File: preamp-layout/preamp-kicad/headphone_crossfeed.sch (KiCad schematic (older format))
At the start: 20 parts

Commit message: BOM Update
parts added to BOM, connector cleanup. Stopping point before renumbering refdes in a more intelligent way.
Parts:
- removed J? (x2): Conn_01x03_Female, Connector_PinHeader_2.54mm:PinHeader_1x03_P2.54mm_Vertical, symbol Connector:Conn_01x03_Female
- added J80, J81: Conn_01x04_Female, symbol Connector:Conn_01x04_Female
- C45, C48: renamed from C?; value 22nF -> 0.022uF
- C46, C47: renamed from C?; value 120nF -> 0.12uF
- gave numbers to parts that had none: 12
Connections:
- net GND: now also J81.2 (Pin_2)
- net L_IN: now also J80.1 (Pin_1)
- net L_OUT: now also J81.1 (Pin_1)
- net R_IN: now also J80.2 (Pin_2)
- net R_OUT: now also J81.3 (Pin_3)
- no-connect marks 0 -> 3

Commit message: Schematic Updates
Updated pin connections for DAC, footprint updates, MCU connections.
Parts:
- C45, C46, C47, C48: footprint (none) -> Capacitor_SMD:C_0805_2012Metric_Pad1.15x1.40mm_HandSolder
- J80, J81: footprint (none) -> Connector_PinHeader_2.54mm:PinHeader_1x04_P2.54mm_Vertical
- R80, R81, R82, R83, R84, R85, R86, R87, R88, R89: footprint (none) -> Resistor_SMD:R_1206_3216Metric_Pad1.42x1.75mm_HandSolder
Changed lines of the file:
@@
 F 0 "R81" H 3920 4196 50  0000 L CNN
 F 1 "1k" H 3920 4105 50  0000 L CNN
-F 2 "" V 3780 4150 50  0001 C CNN
+F 2 "Resistor_SMD:R_1206_3216Metric_Pad1.42x1.75mm_HandSolder" V 3780 4150 50  0001 C CNN
 F 3 "~" H 3850 4150 50  0001 C CNN
 	1    3850 4150
@@
 F 0 "R82" H 4420 3696 50  0000 L CNN
 F 1 "9.1k" H 4420 3605 50  0000 L CNN
-F 2 "" V 4280 3650 50  0001 C CNN
+F 2 "Resistor_SMD:R_1206_3216Metric_Pad1.42x1.75mm_HandSolder" V 4280 3650 50  0001 C CNN
 F 3 "~" H 4350 3650 50  0001 C CNN
 	1    4350 3650
@@
 F 0 "R83" V 5307 2700 50  0000 C CNN
 F 1 "3.3k" V 5216 2700 50  0000 C CNN
-F 2 "" V 5030 2700 50  0001 C CNN
+F 2 "Resistor_SMD:R_1206_3216Metric_Pad1.42x1.75mm_HandSolder" V 5030 2700 50  0001 C CNN
 F 3 "~" H 5100 2700 50  0001 C CNN
 	1    5100 2700
@@
 F 0 "C45" H 4465 3196 50  0000 L CNN
 F 1 "0.022uF" H 4465 3105 50  0000 L CNN
-F 2 "" H 4388 3000 50  0001 C CNN
+F 2 "Capacitor_SMD:C_0805_2012Metric_Pad1.15x1.40mm_HandSolder" H 4388 3000 50  0001 C CNN
 F 3 "~" H 4350 3150 50  0001 C CNN
 	1    4350 3150
@@
 F 0 "C46" H 5465 2996 50  0000 L CNN
 F 1 "0.12uF" H 5465 2905 50  0000 L CNN
-F 2 "" H 5388 2800 50  0001 C CNN
+F 2 "Capacitor_SMD:C_0805_2012Metric_Pad1.15x1.40mm_HandSolder" H 5388 2800 50  0001 C CNN
 F 3 "~" H 5350 2950 50  0001 C CNN
 	1    5350 2950
@@
 F 0 "R84" V 5807 2700 50  0000 C CNN
 F 1 "3.3k" V 5716 2700 50  0000 C CNN
-F 2 "" V 5530 2700 50  0001 C CNN
+F 2 "Resistor_SMD:R_1206_3216Metric_Pad1.42x1.75mm_HandSolder" V 5530 2700 50  0001 C CNN
 F 3 "~" H 5600 2700 50  0001 C CNN
 	1    5600 2700
@@
 F 0 "R80" H 3920 3696 50  0000 L CNN
 F 1 "1.5k" H 3920 3605 50  0000 L CNN
-F 2 "" V 3780 3650 50  0001 C CNN
+F 2 "Resistor_SMD:R_1206_3216Metric_Pad1.42x1.75mm_HandSolder" V 3780 3650 50  0001 C CNN
 F 3 "~" H 3850 3650 50  0001 C CNN
 	1    3850 3650
@@
 F 0 "R89" H 8130 4196 50  0000 R CNN
 F 1 "1k" H 8130 4105 50  0000 R CNN
-F 2 "" V 8130 4150 50  0001 C CNN
+F 2 "Resistor_SMD:R_1206_3216Metric_Pad1.42x1.75mm_HandSolder" V 8130 4150 50  0001 C CNN
 F 3 "~" H 8200 4150 50  0001 C CNN
 	1    8200 4150
@@
 F 0 "R87" H 7630 3696 50  0000 R CNN
 F 1 "9.1k" H 7630 3605 50  0000 R CNN
-F 2 "" V 7630 3650 50  0001 C CNN
+F 2 "Resistor_SMD:R_1206_3216Metric_Pad1.42x1.75mm_HandSolder" V 7630 3650 50  0001 C CNN
 F 3 "~" H 7700 3650 50  0001 C CNN
 	1    7700 3650
@@
 F 0 "R86" V 7157 2700 50  0000 C CNN
 F 1 "3.3k" V 7066 2700 50  0000 C CNN
-F 2 "" V 6880 2700 50  0001 C CNN
+F 2 "Resistor_SMD:R_1206_3216Metric_Pad1.42x1.75mm_HandSolder" V 6880 2700 50  0001 C CNN
 F 3 "~" H 6950 2700 50  0001 C CNN
 	1    6950 2700
@@
 F 0 "C48" H 7814 3196 50  0000 L CNN
 F 1 "0.022uF" H 7814 3105 50  0000 L CNN
-F 2 "" H 7738 3000 50  0001 C CNN
+F 2 "Capacitor_SMD:C_0805_2012Metric_Pad1.15x1.40mm_HandSolder" H 7738 3000 50  0001 C CNN
 F 3 "~" H 7700 3150 50  0001 C CNN
 	1    7700 3150
@@
 F 0 "C47" H 6585 2996 50  0000 R CNN
 F 1 "0.12uF" H 6585 2905 50  0000 R CNN
-F 2 "" H 6738 2800 50  0001 C CNN
+F 2 "Capacitor_SMD:C_0805_2012Metric_Pad1.15x1.40mm_HandSolder" H 6738 2800 50  0001 C CNN
 F 3 "~" H 6700 2950 50  0001 C CNN
 	1    6700 2950
@@
 F 0 "R85" V 6657 2700 50  0000 C CNN
 F 1 "3.3k" V 6566 2700 50  0000 C CNN
-F 2 "" V 6380 2700 50  0001 C CNN
+F 2 "Resistor_SMD:R_1206_3216Metric_Pad1.42x1.75mm_HandSolder" V 6380 2700 50  0001 C CNN
 F 3 "~" H 6450 2700 50  0001 C CNN
 	1    6450 2700
@@
 F 0 "R88" H 8130 3696 50  0000 R CNN
 F 1 "1.5k" H 8130 3605 50  0000 R CNN
-F 2 "" V 8130 3650 50  0001 C CNN
+F 2 "Resistor_SMD:R_1206_3216Metric_Pad1.42x1.75mm_HandSolder" V 8130 3650 50  0001 C CNN
 F 3 "~" H 8200 3650 50  0001 C CNN
 	1    8200 3650
@@
 F 0 "J80" H 3628 5780 50  0000 L CNN
 F 1 "Conn_01x04_Female" H 3628 5735 50  0001 L CNN
-F 2 "" H 3600 5850 50  0001 C CNN
+F 2 "Connector_PinHeader_2.54mm:PinHeader_1x04_P2.54mm_Vertical" H 3600 5850 50  0001 C CNN
 F 3 "~" H 3600 5850 50  0001 C CNN
 	1    3600 5850
@@
 F 0 "J81" H 4142 6043 50  0000 C CNN
 F 1 "Conn_01x04_Female" H 4278 5735 50  0001 L CNN
-F 2 "" H 4250 5850 50  0001 C CNN
+F 2 "Connector_PinHeader_2.54mm:PinHeader_1x04_P2.54mm_Vertical" H 4250 5850 50  0001 C CNN
 F 3 "~" H 4250 5850 50  0001 C CNN
 	1    4250 5850

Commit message: Schematic Redesignation
Regenerated RefDes for all parts, updated BOM accordingly and perfomred check on values, RefDes present from schematic to BOM. Value changes, BOM filled in as a result.
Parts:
- removed J81: Conn_01x04_Female, Connector_PinHeader_2.54mm:PinHeader_1x04_P2.54mm_Vertical, symbol Connector:Conn_01x04_Female
- added J79: Conn_01x04_Male, Connector_PinHeader_2.54mm:PinHeader_1x04_P2.54mm_Vertical, symbol Connector:Conn_01x04_Male
- renumbered J80 to J78
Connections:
- net GND: now also J79.2 (Pin_2)
- net L_OUT: now also J79.1 (Pin_1)
- net R_OUT: now also J79.3 (Pin_3)
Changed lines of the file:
@@
 AR Path="/5E4A803E/5EE90DB9" Ref="SW?"  Part="1"
 AR Path="/5E4A803E/5EE80145/5EE90DB9" Ref="SW12"  Part="1"
-F 0 "SW12" V 4554 2612 50  0000 R CNN
-F 1 "SW_DPDT_x2" V 4645 2612 50  0000 R CNN
+F 0 "SW12" H 4600 2567 50  0000 C CNN
+F 1 "SW_DPDT_x2" V 4645 2612 50  0001 R CNN
 F 2 "" H 4600 2800 50  0001 C CNN
 F 3 "~" H 4600 2800 50  0001 C CNN
@@
 AR Path="/5E4A803E/5EE90DBF" Ref="SW?"  Part="2"
 AR Path="/5E4A803E/5EE80145/5EE90DBF" Ref="SW12"  Part="2"
-F 0 "SW12" V 7404 2613 50  0000 R CNN
-F 1 "SW_DPDT_x2" V 7495 2613 50  0000 R CNN
+F 0 "SW12" H 7450 2567 50  0000 C CNN
+F 1 "SW_DPDT_x2" V 7495 2613 50  0001 R CNN
 F 2 "" H 7450 2800 50  0001 C CNN
 F 3 "~" H 7450 2800 50  0001 C CNN
@@
 AR Path="/5E4A803E/5EE90E02" Ref="C?"  Part="1"
 AR Path="/5E4A803E/5EE80145/5EE90E02" Ref="C48"  Part="1"
-F 0 "C48" H 7814 3196 50  0000 L CNN
-F 1 "0.022uF" H 7814 3105 50  0000 L CNN
+F 0 "C48" H 7815 3196 50  0000 L CNN
+F 1 "0.022uF" H 7815 3105 50  0000 L CNN
 F 2 "Capacitor_SMD:C_0805_2012Metric_Pad1.15x1.40mm_HandSolder" H 7738 3000 50  0001 C CNN
 F 3 "~" H 7700 3150 50  0001 C CNN
@@
 R_OUT
 $Comp
-L Connector:Conn_01x04_Female J80
+L Connector:Conn_01x04_Female J78
 U 1 1 5E7CDD58
 P 3600 5850
-F 0 "J80" H 3628 5780 50  0000 L CNN
+F 0 "J78" H 3628 5780 50  0000 L CNN
 F 1 "Conn_01x04_Female" H 3628 5735 50  0001 L CNN
 F 2 "Connector_PinHeader_2.54mm:PinHeader_1x04_P2.54mm_Vertical" H 3600 5850 50  0001 C CNN
@@
 	1    3600 5850
 	1    0    0    -1
-$EndComp
-$Comp
-L Connector:Conn_01x04_Female J81
-U 1 1 5E7CF489
-P 4250 5850
-F 0 "J81" H 4142 6043 50  0000 C CNN
-F 1 "Conn_01x04_Female" H 4278 5735 50  0001 L CNN
-F 2 "Connector_PinHeader_2.54mm:PinHeader_1x04_P2.54mm_Vertical" H 4250 5850 50  0001 C CNN
-F 3 "~" H 4250 5850 50  0001 C CNN
-	1    4250 5850
-	-1   0    0    -1
 $EndComp
 NoConn ~ 4450 6050
@@
 Wire Wire Line
 	4450 5850 4800 5850
+$Comp
+L Connector:Conn_01x04_Male J79
+U 1 1 5EF52177
+P 4250 5850
+F 0 "J79" H 4358 6039 50  0000 C CNN
+F 1 "Conn_01x04_Male" H 4358 6040 50  0001 C CNN
+F 2 "Connector_PinHeader_2.54mm:PinHeader_1x04_P2.54mm_Vertical" H 4250 5850 50  0001 C CNN
+F 3 "~" H 4250 5850 50  0001 C CNN
+	1    4250 5850
+	1    0    0    -1
+$EndComp
 $EndSCHEMATC

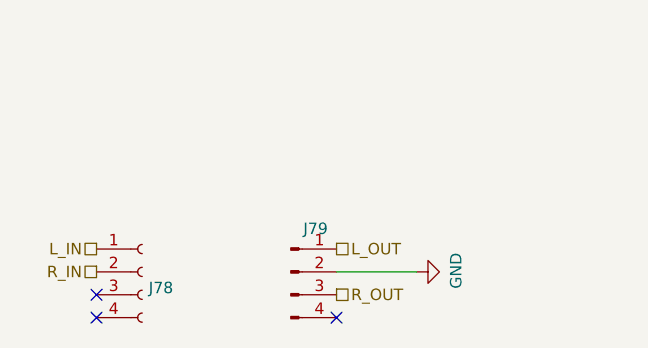
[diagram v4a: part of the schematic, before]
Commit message: Headphone Amp Update
Removed IC buffer on headphone amp schematic. Reconfigured connectors to crossfeed board so that input/output can be easily jumpered.
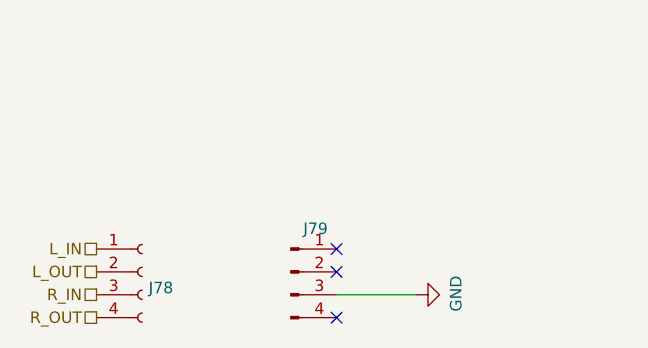
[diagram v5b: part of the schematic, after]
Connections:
- net GND: now also J79.3 (Pin_3); no longer J79.2 (Pin_2)
- net L_OUT: now also J78.2 (Pin_2); no longer J79.1 (Pin_1)
- net R_IN: now also J78.3 (Pin_3); no longer J78.2 (Pin_2)
- net R_OUT: now also J78.4 (Pin_4); no longer J79.3 (Pin_3)
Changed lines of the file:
@@
 Text HLabel 3400 5750 0    50   UnSpc ~ 0
 L_IN
-Text HLabel 4450 5750 2    50   UnSpc ~ 0
-L_OUT
-Text HLabel 3400 5850 0    50   UnSpc ~ 0
-R_IN
-Text HLabel 4450 5950 2    50   UnSpc ~ 0
-R_OUT
 $Comp
 L Connector:Conn_01x04_Female J78
@@
 $EndComp
 NoConn ~ 4450 6050
-NoConn ~ 3400 5950
-NoConn ~ 3400 6050
-$Comp
-L power:GND #PWR?
-U 1 1 5E7DF118
-P 4800 5850
-AR Path="/6009D432/5E7DF118" Ref="#PWR?"  Part="1"
-AR Path="/5E4A803E/5E7DF118" Ref="#PWR?"  Part="1"
-AR Path="/5E4A803E/5EE80145/5E7DF118" Ref="#PWR0115"  Part="1"
-F 0 "#PWR0115" H 4800 5600 50  0001 C CNN
-F 1 "GND" H 4805 5677 50  0000 C CNN
-F 2 "" H 4800 5850 50  0001 C CNN
-F 3 "" H 4800 5850 50  0001 C CNN
-	1    4800 5850
-	0    -1   -1   0
-$EndComp
-Wire Wire Line
-	4450 5850 4800 5850
 $Comp
 L Connector:Conn_01x04_Male J79
@@
 	1    0    0    -1
 $EndComp
+Text HLabel 3400 5950 0    50   UnSpc ~ 0
+R_IN
+Text HLabel 3400 5850 0    50   UnSpc ~ 0
+L_OUT
+Text HLabel 3400 6050 0    50   UnSpc ~ 0
+R_OUT
+$Comp
+L power:GND #PWR?
+U 1 1 5E7DF118
+P 4800 5950
+AR Path="/6009D432/5E7DF118" Ref="#PWR?"  Part="1"
+AR Path="/5E4A803E/5E7DF118" Ref="#PWR?"  Part="1"
+AR Path="/5E4A803E/5EE80145/5E7DF118" Ref="#PWR0115"  Part="1"
+F 0 "#PWR0115" H 4800 5700 50  0001 C CNN
+F 1 "GND" H 4805 5777 50  0000 C CNN
+F 2 "" H 4800 5950 50  0001 C CNN
+F 3 "" H 4800 5950 50  0001 C CNN
+	1    4800 5950
+	0    -1   -1   0
+$EndComp
+Wire Wire Line
+	4450 5950 4800 5950
+NoConn ~ 4450 5750
+NoConn ~ 4450 5850
 $EndSCHEMATC
